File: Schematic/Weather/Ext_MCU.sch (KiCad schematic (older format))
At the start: 5 parts, among them J14 4_Way_Wire, J15 4_Way_Wire, J16 4_Way_Wire, U2 AMS1117, U3 ESP-01v090

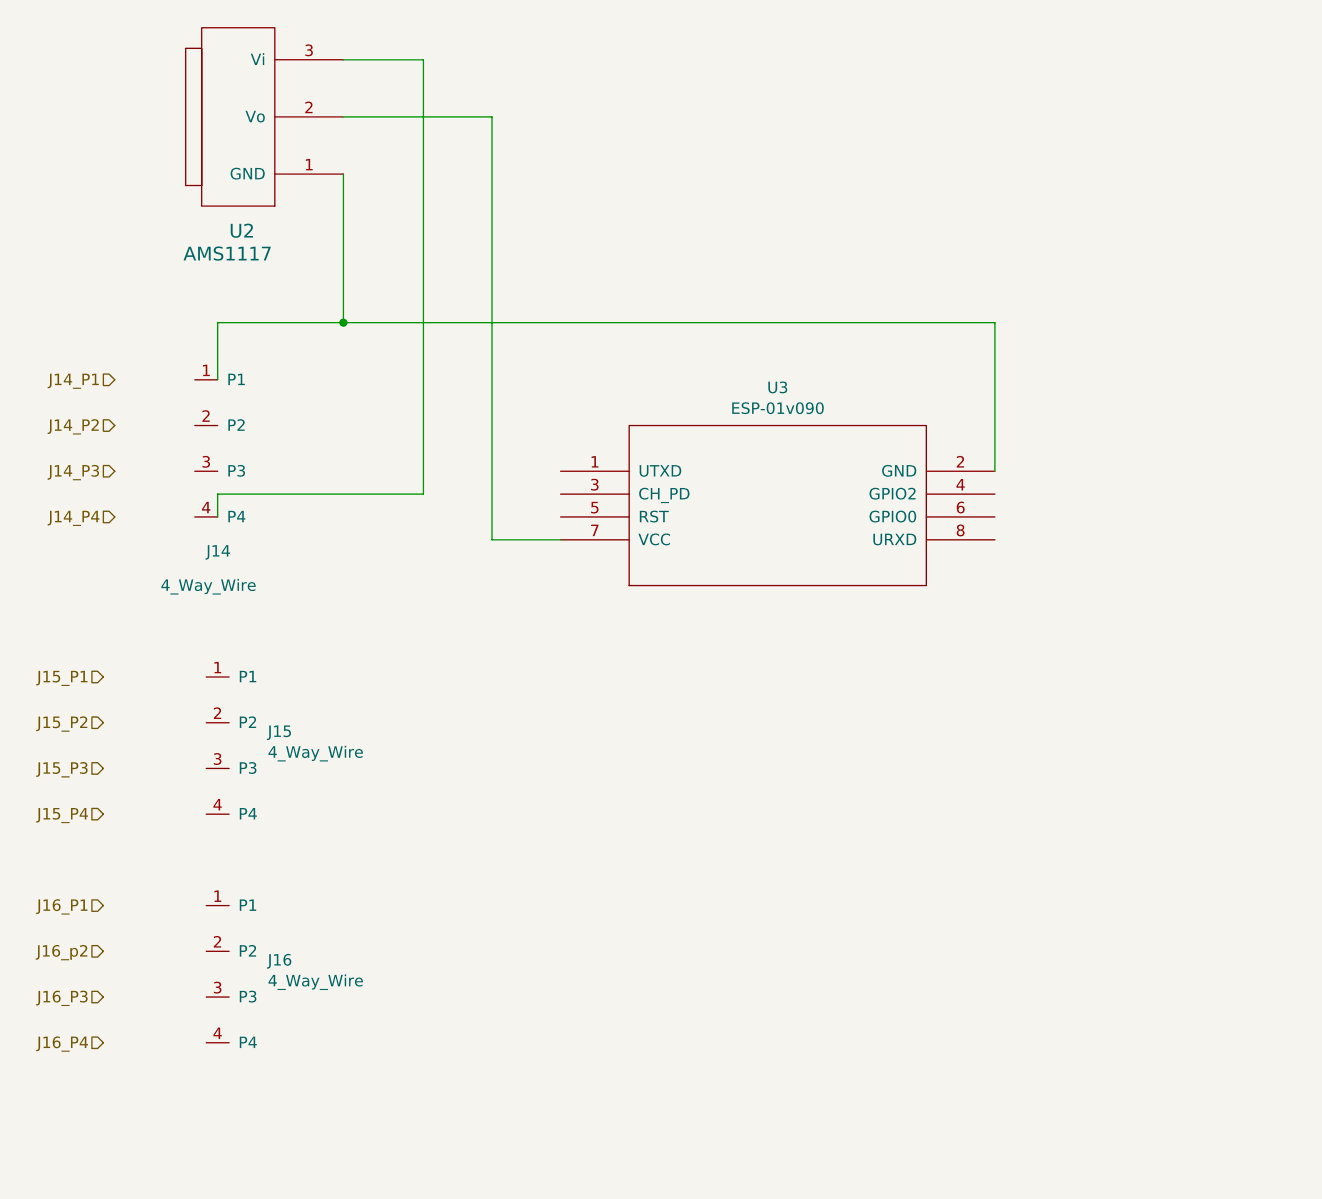
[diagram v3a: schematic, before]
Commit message: config connectors sda scl
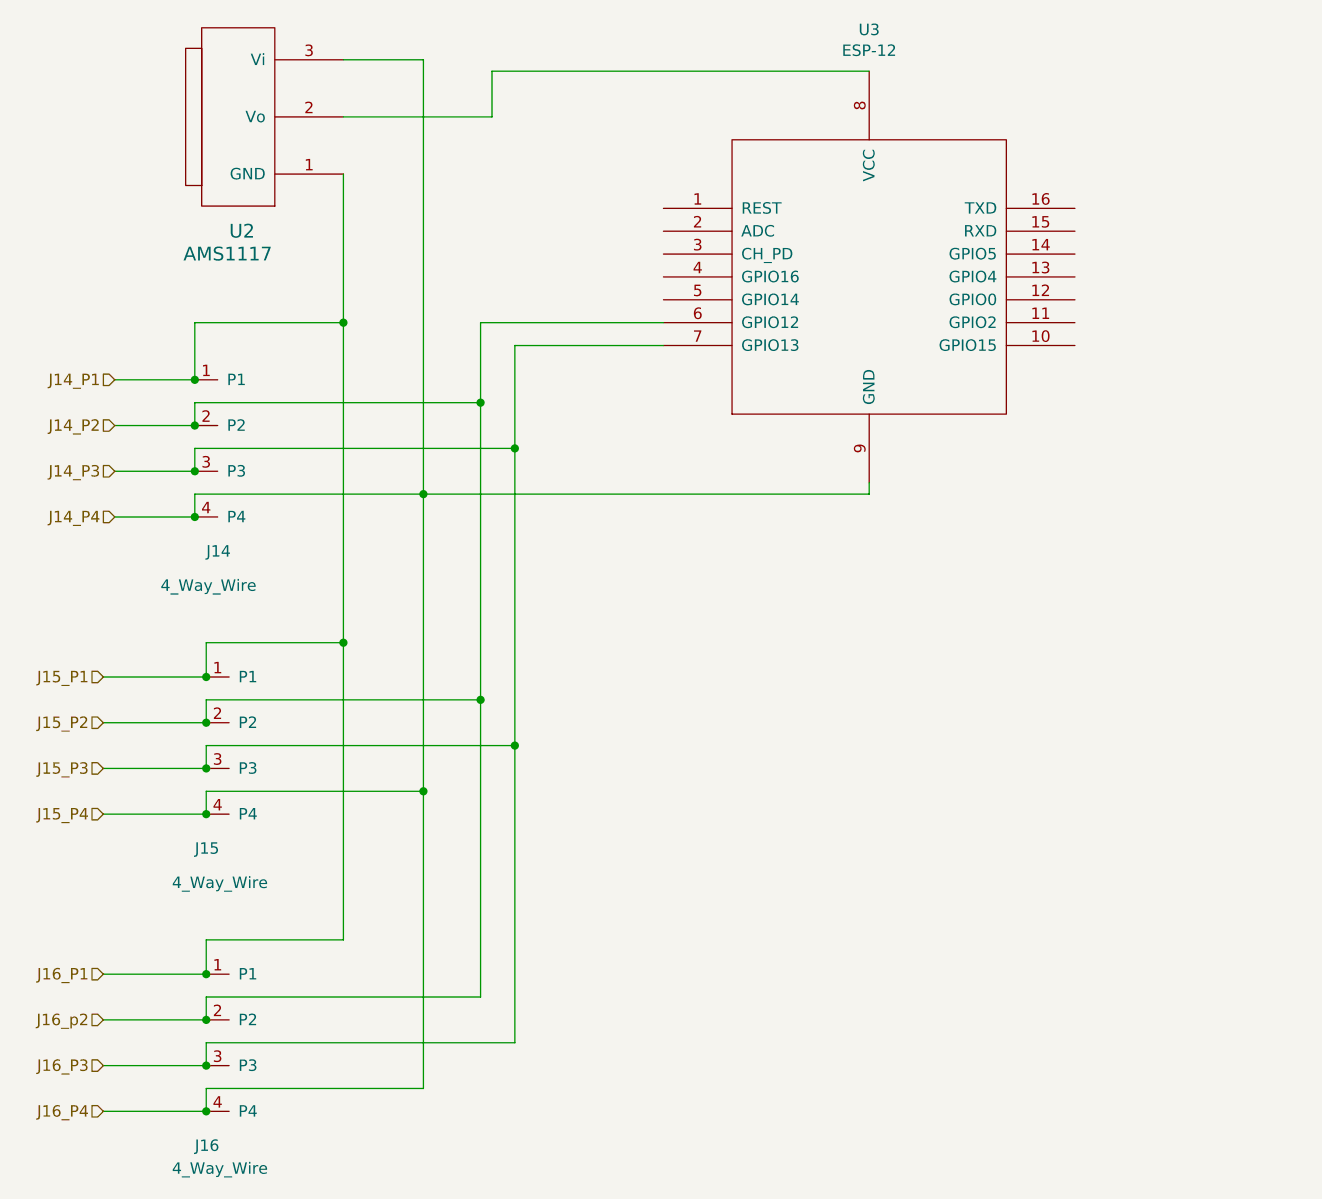
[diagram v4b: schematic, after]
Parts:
- removed U3: ESP-01v090, footprint:ESP-01, symbol Weather-rescue:ESP-01v090-ESP8266
- added U3: ESP-12, symbol ESP8266:ESP-12
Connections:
- wire segments 12 -> 56
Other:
- moved on the sheet: J16
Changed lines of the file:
@@
 Text HLabel 2600 5000 0    50   Input ~ 0
 J15_P4
-Text HLabel 2600 5400 0    50   Input ~ 0
+Text HLabel 2600 5700 0    50   Input ~ 0
 J16_P1
-Text HLabel 2600 5600 0    50   Input ~ 0
+Text HLabel 2600 5900 0    50   Input ~ 0
 J16_p2
-Text HLabel 2600 5800 0    50   Input ~ 0
+Text HLabel 2600 6100 0    50   Input ~ 0
 J16_P3
-Text HLabel 2600 6000 0    50   Input ~ 0
+Text HLabel 2600 6300 0    50   Input ~ 0
 J16_P4
-$Comp
-L Weather-rescue:ESP-01v090-ESP8266 U?
-U 1 1 5C950A1B
-P 5550 3650
-AR Path="/5C950A1B" Ref="U?"  Part="1"
-AR Path="/5C93D4CF/5C950A1B" Ref="U3"  Part="1"
-F 0 "U3" H 5550 4165 50  0000 C CNN
-F 1 "ESP-01v090" H 5550 4074 50  0000 C CNN
-F 2 "footprint:ESP-01" H 5550 3650 50  0001 C CNN
-F 3 "http://l0l.org.uk/2014/12/esp8266-modules-hardware-guide-gotta-catch-em-all/" H 5550 3650 50  0001 C CNN
-	1    5550 3650
-	1    0    0    -1
-$EndComp
 $Comp
 L MyComponents:4_Way_Wire J14
@@
 $EndComp
 Wire Wire Line
-	6500 3500 6500 2850
-Wire Wire Line
-	6500 2850 3650 2850
-Wire Wire Line
-	3100 2850 3100 3100
-Wire Wire Line
 	3650 2200 3650 2850
-Connection ~ 3650 2850
-Wire Wire Line
-	3650 2850 3100 2850
 Wire Wire Line
 	3650 1700 4000 1700
@@
 	4000 1700 4000 3600
 Wire Wire Line
-	4000 3600 3100 3600
-Wire Wire Line
-	3100 3600 3100 3700
-Wire Wire Line
 	3650 1950 4300 1950
-Wire Wire Line
-	4300 1950 4300 3800
-Wire Wire Line
-	4300 3800 4600 3800
 $Comp
 L MyComponents:4_Way_Wire J15
 U 1 1 5CB477D0
 P 3150 4400
-F 0 "J15" H 3319 4161 50  0000 L CNN
-F 1 "4_Way_Wire" H 3319 4070 50  0000 L CNN
+F 0 "J15" H 3000 3650 50  0000 L CNN
+F 1 "4_Way_Wire" H 2900 3500 50  0000 L CNN
 F 2 "Connector_PinHeader_2.54mm:PinHeader_1x04_P2.54mm_Vertical" H 3050 4450 50  0001 C CNN
 F 3 "" H 3050 4450 50  0001 C CNN
@@
 L MyComponents:4_Way_Wire J16
 U 1 1 5CB50010
-P 3150 5400
-F 0 "J16" H 3319 5161 50  0000 L CNN
-F 1 "4_Way_Wire" H 3319 5070 50  0000 L CNN
-F 2 "Connector_PinHeader_2.54mm:PinHeader_1x04_P2.54mm_Vertical" H 3050 5450 50  0001 C CNN
-F 3 "" H 3050 5450 50  0001 C CNN
-	1    3150 5400
+P 3150 5700
+F 0 "J16" H 3000 4950 50  0000 L CNN
+F 1 "4_Way_Wire" H 2900 4850 50  0000 L CNN
+F 2 "Connector_PinHeader_2.54mm:PinHeader_1x04_P2.54mm_Vertical" H 3050 5750 50  0001 C CNN
+F 3 "" H 3050 5750 50  0001 C CNN
+	1    3150 5700
 	1    0    0    -1
 $EndComp
+Wire Wire Line
+	3000 3100 3000 2850
+Wire Wire Line
+	3000 2850 3650 2850
+Wire Wire Line
+	3000 3700 3000 3600
+Wire Wire Line
+	3000 3600 4000 3600
+$Comp
+L ESP8266:ESP-12 U3
+U 1 1 5CB467A8
+P 5950 2650
+F 0 "U3" H 5950 3731 50  0000 C CNN
+F 1 "ESP-12" H 5950 3640 50  0000 C CNN
+F 2 "" H 5950 2650 50  0001 C CNN
+F 3 "http://l0l.org.uk/2014/12/esp8266-modules-hardware-guide-gotta-catch-em-all/" H 5950 2650 50  0001 C CNN
+	1    5950 2650
+	1    0    0    -1
+$EndComp
+Wire Wire Line
+	4300 1950 4300 1750
+Wire Wire Line
+	4300 1750 5950 1750
+Wire Wire Line
+	4000 3600 5950 3600
+Wire Wire Line
+	5950 3600 5950 3550
+Connection ~ 4000 3600
+Wire Wire Line
+	5050 2850 4250 2850
+Wire Wire Line
+	4250 2850 4250 3200
+Wire Wire Line
+	4250 3200 3000 3200
+Wire Wire Line
+	3000 3200 3000 3300
+Wire Wire Line
+	3000 3500 3000 3400
+Wire Wire Line
+	3000 3400 4400 3400
+Wire Wire Line
+	4400 3400 4400 2950
+Wire Wire Line
+	4400 2950 5050 2950
+Wire Wire Line
+	3650 2850 3650 4250
+Wire Wire Line
+	3650 4250 3050 4250
+Wire Wire Line
+	3050 4250 3050 4400
+Connection ~ 3650 2850
+Wire Wire Line
+	3650 4250 3650 5550
+Wire Wire Line
+	3650 5550 3050 5550
+Wire Wire Line
+	3050 5550 3050 5700
+Connection ~ 3650 4250
+Wire Wire Line
+	4000 3600 4000 4900
+Wire Wire Line
+	4000 4900 3050 4900
+Wire Wire Line
+	3050 4900 3050 5000
+Wire Wire Line
+	4000 4900 4000 6200
+Wire Wire Line
+	4000 6200 3050 6200
+Wire Wire Line
+	3050 6200 3050 6300
+Connection ~ 4000 4900
+Wire Wire Line
+	4250 3200 4250 4500
+Wire Wire Line
+	4250 4500 3050 4500
+Wire Wire Line
+	3050 4500 3050 4600
+Connection ~ 4250 3200
+Wire Wire Line
+	4400 3400 4400 4700
+Wire Wire Line
+	4400 4700 3050 4700
+Wire Wire Line
+	3050 4700 3050 4800
+Connection ~ 4400 3400
+Wire Wire Line
+	4250 4500 4250 5800
+Wire Wire Line
+	4250 5800 3050 5800
+Wire Wire Line
+	3050 5800 3050 5900
+Connection ~ 4250 4500
+Wire Wire Line
+	4400 4700 4400 6000
+Wire Wire Line
+	4400 6000 3050 6000
+Wire Wire Line
+	3050 6000 3050 6100
+Connection ~ 4400 4700
+Wire Wire Line
+	2600 6300 3050 6300
+Connection ~ 3050 6300
+Wire Wire Line
+	2600 6100 3050 6100
+Connection ~ 3050 6100
+Wire Wire Line
+	2600 5900 3050 5900
+Connection ~ 3050 5900
+Wire Wire Line
+	2600 5700 3050 5700
+Connection ~ 3050 5700
+Wire Wire Line
+	2600 5000 3050 5000
+Connection ~ 3050 5000
+Wire Wire Line
+	2600 4800 3050 4800
+Connection ~ 3050 4800
+Wire Wire Line
+	2600 4600 3050 4600
+Connection ~ 3050 4600
+Wire Wire Line
+	2600 4400 3050 4400
+Connection ~ 3050 4400
+Wire Wire Line
+	2650 3100 3000 3100
+Connection ~ 3000 3100
+Wire Wire Line
+	2650 3300 3000 3300
+Connection ~ 3000 3300
+Wire Wire Line
+	2650 3500 3000 3500
+Connection ~ 3000 3500
+Wire Wire Line
+	2650 3700 3000 3700
+Connection ~ 3000 3700
 $EndSCHEMATC

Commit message: Local webpage added
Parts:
- U3: footprint (none) -> footprint:ESP-12_breakout
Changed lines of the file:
@@
 F 0 "U3" H 5950 3731 50  0000 C CNN
 F 1 "ESP-12" H 5950 3640 50  0000 C CNN
-F 2 "" H 5950 2650 50  0001 C CNN
+F 2 "footprint:ESP-12_breakout" H 5950 2650 50  0001 C CNN
 F 3 "http://l0l.org.uk/2014/12/esp8266-modules-hardware-guide-gotta-catch-em-all/" H 5950 2650 50  0001 C CNN
 	1    5950 2650
